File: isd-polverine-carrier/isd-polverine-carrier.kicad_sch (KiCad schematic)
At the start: 21 parts, among them J1 BATT, J3 Conn_01x02_Pin, J4 Conn_01x08_Socket, J5 Conn_01x08_Socket, Q1 Q_Dual_NMOS_S1G1D2S2G2D1, U1 DW01A, U5 AP2112K-3.3, U6 MCP73831-2-OT

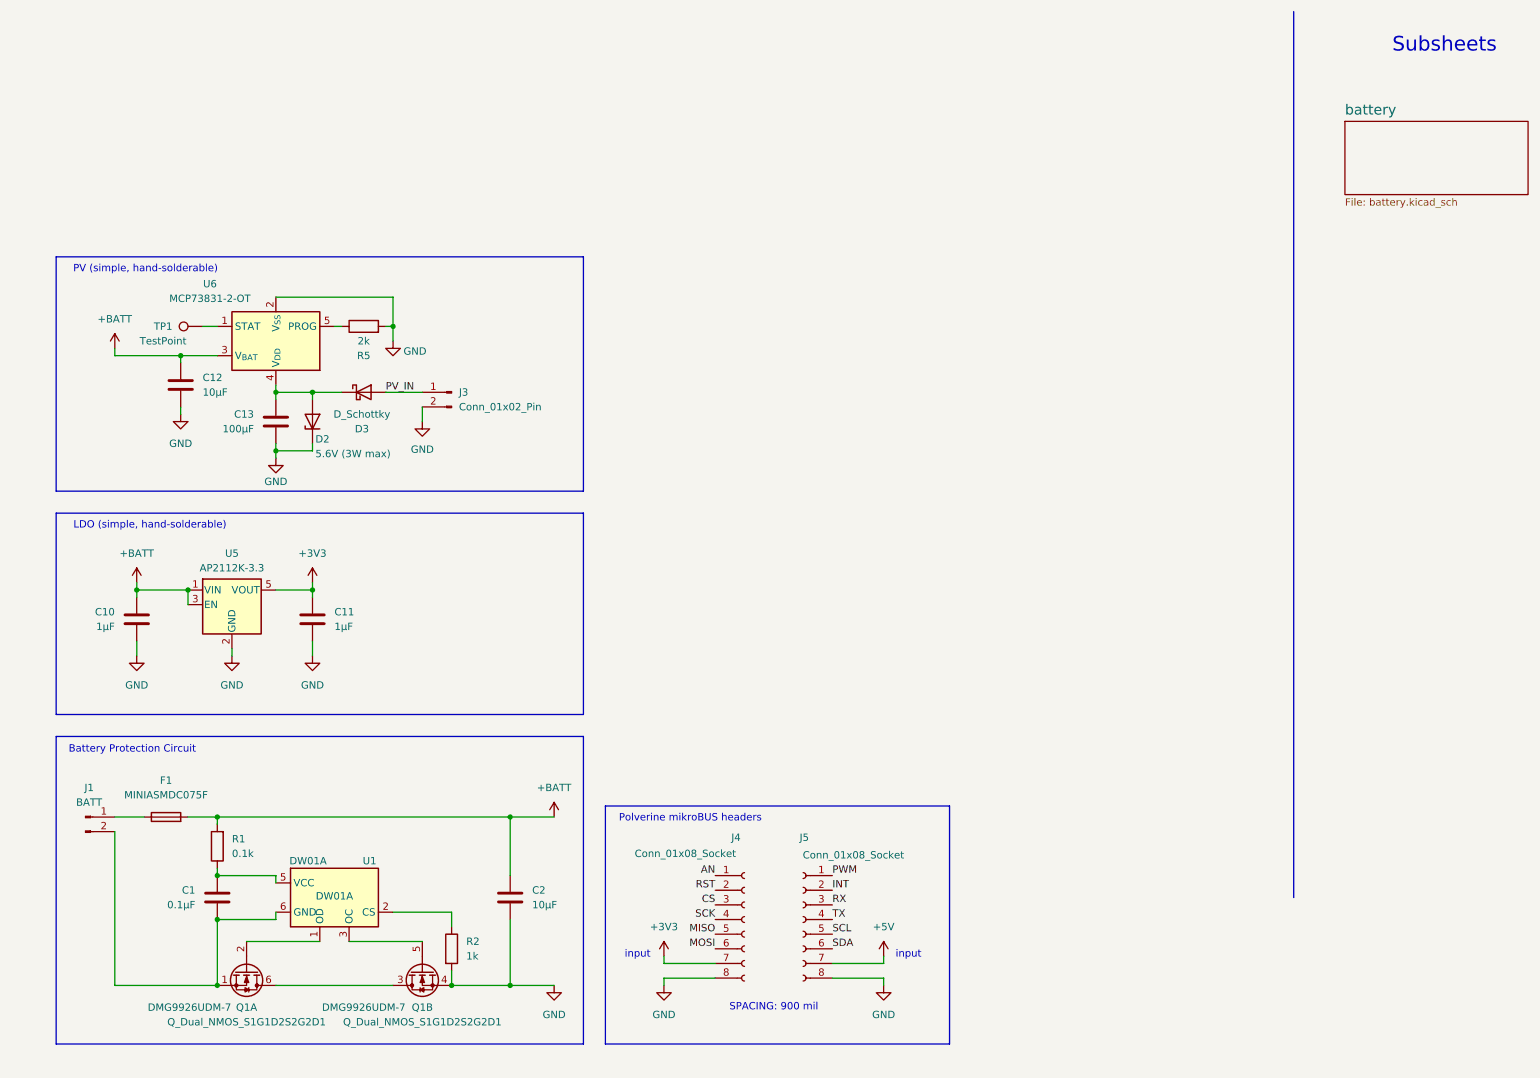
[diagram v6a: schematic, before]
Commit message: add: USB-port for charging, carrier headers, battery monitoring
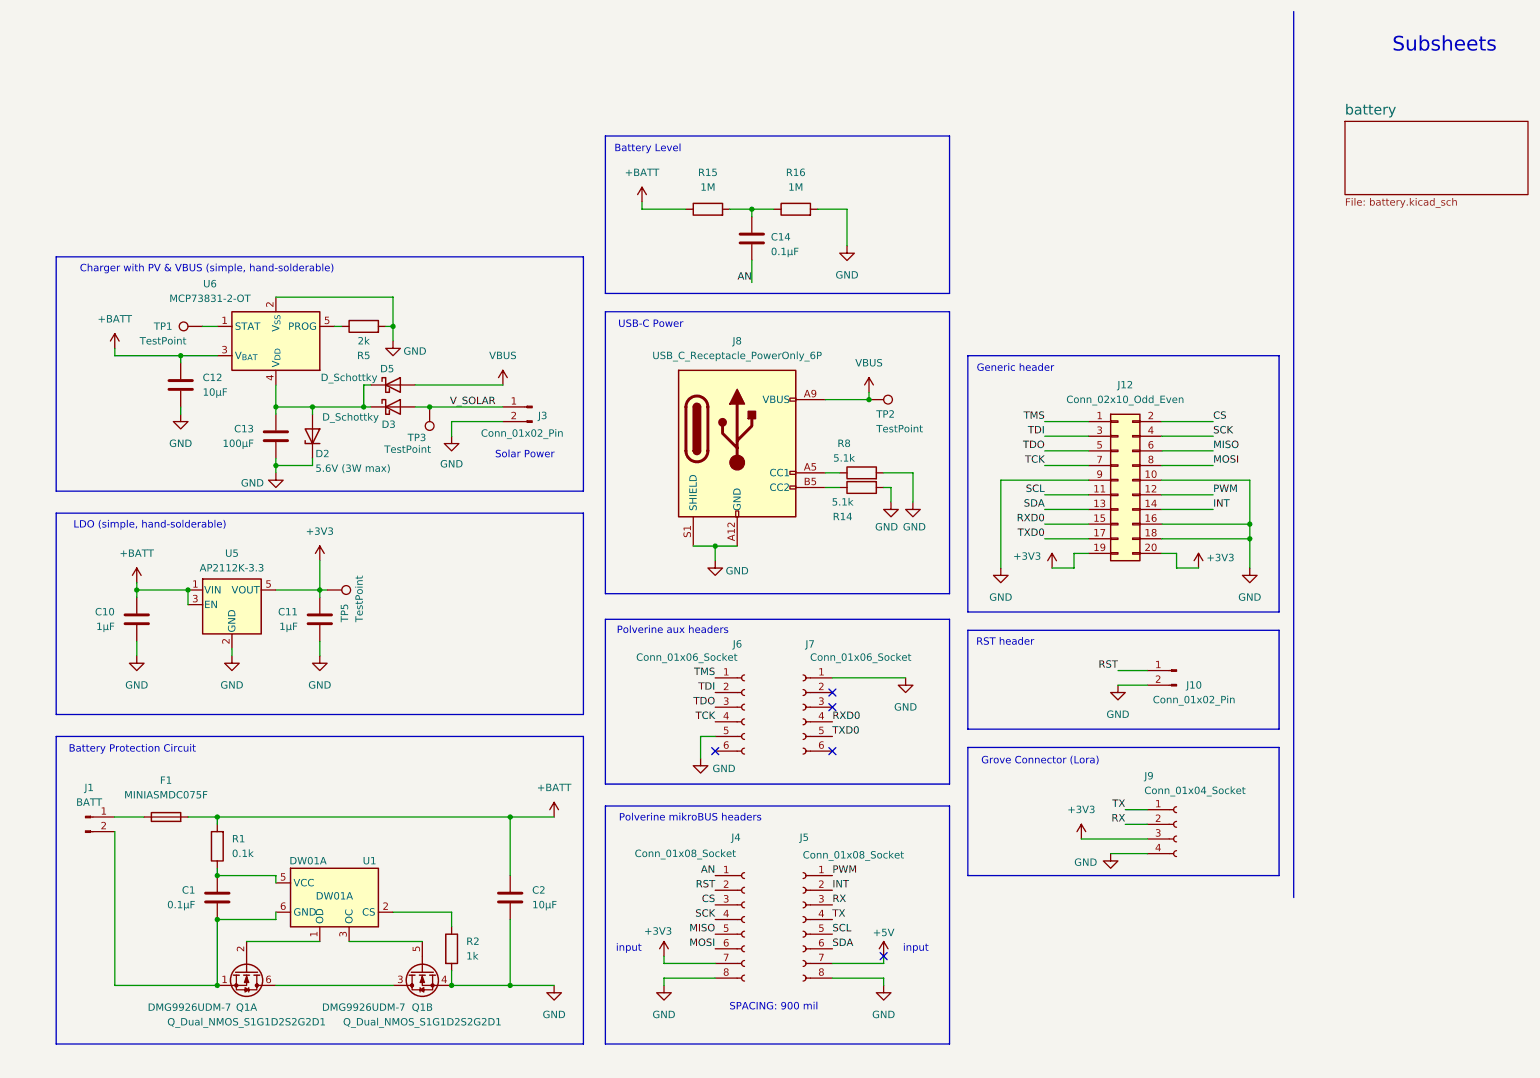
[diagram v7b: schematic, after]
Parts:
- added C14: 0.1µF, symbol Device:C
- added D5: D_Schottky, symbol Device:D_Schottky
- added J10: Conn_01x02_Pin, Connector_PinHeader_2.54mm:PinHeader_1x02_P2.54mm_Vertical, symbol Connector:Conn_01x02_Pin
- added J12: Conn_02x10_Odd_Even, symbol Connector_Generic:Conn_02x10_Odd_Even
- added J6, J7: Conn_01x06_Socket, symbol Connector:Conn_01x06_Socket
- added J8: USB_C_Receptacle_PowerOnly_6P, Connector_USB:USB_C_Receptacle_GCT_USB4125-xx-x-0190_6P_TopMnt_Horizontal, symbol Connector:USB_C_Receptacle_PowerOnly_6P
- added J9: Conn_01x04_Socket, Connector:NS-Tech_Grove_1x04_P2mm_Vertical, symbol Connector:Conn_01x04_Socket
- added R14, R8: 5.1k, symbol Device:R
- added R15, R16: 1M, symbol Device:R
- added TP2, TP3, TP5: TestPoint, symbol Connector:TestPoint
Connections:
- net +3V3: now also J12.19 (Pin_19), J12.20 (Pin_20), J9.3 (Pin_3), TP5.1
- net +BATT: now also R15.1
- net AN: now also C14.2
- net CS: now also J12.2 (Pin_2)
- net GND: now also J10.2 (Pin_2), J12.10 (Pin_10), J12.16 (Pin_16), J12.18 (Pin_18), J12.9 (Pin_9), J6.5 (Pin_5), J7.1 (Pin_1), J8.A12 (GND), J8.B12 (GND), J8.S1 (SHIELD), J9.4 (Pin_4), R14.2, R16.2, R8.2
- net INT: now also J12.14 (Pin_14)
- net MISO: now also J12.6 (Pin_6)
- net MOSI: now also J12.8 (Pin_8)
- net PWM: now also J12.12 (Pin_12)
- net RST: now also J10.1 (Pin_1)
- net RX: now also J9.2 (Pin_2)
- net SCK: now also J12.4 (Pin_4)
- net SCL: now also J12.11 (Pin_11)
- net SDA: now also J12.13 (Pin_13)
- net TX: now also J9.1 (Pin_1)
- net at C13.1, D2.2 (A), D3.1 (K)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: now also D5.1 (K)
- net PV_IN renamed V_SOLAR
- net V_SOLAR: now also TP3.1
- new net: C14.1, R15.2, R16.1
- new net: J8.A5 (CC1), R8.1
- new net: J8.B5 (CC2), R14.1
- new net RXD0: J12.15 (Pin_15), J7.4 (Pin_4)
- new net TCK: J12.7 (Pin_7), J6.4 (Pin_4)
- new net TDI: J12.3 (Pin_3), J6.2 (Pin_2)
- new net TDO: J12.5 (Pin_5), J6.3 (Pin_3)
- new net TMS: J12.1 (Pin_1), J6.1 (Pin_1)
- new net TXD0: J12.17 (Pin_17), J7.5 (Pin_5)
- new net VBUS: D5.2 (A), J8.A9 (VBUS), J8.B9 (VBUS), TP2.1
- no-connect marks 0 -> 5
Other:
- note added: "Battery Level"
- note added: "Charger with PV & VBUS (simple, hand-solderable)"
- note added: "Generic header"
- note added: "Grove Connector (Lora)"
- note added: "Polverine aux headers"
- note added: "RST header"
- note added: "Solar Power"
- note added: "USB-C Power"
- note removed: "PV (simple, hand-solderable)"
- moved on the sheet: C11, C13, D2, D3, J3

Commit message: Added P Mos to solar charger controller for load sharing
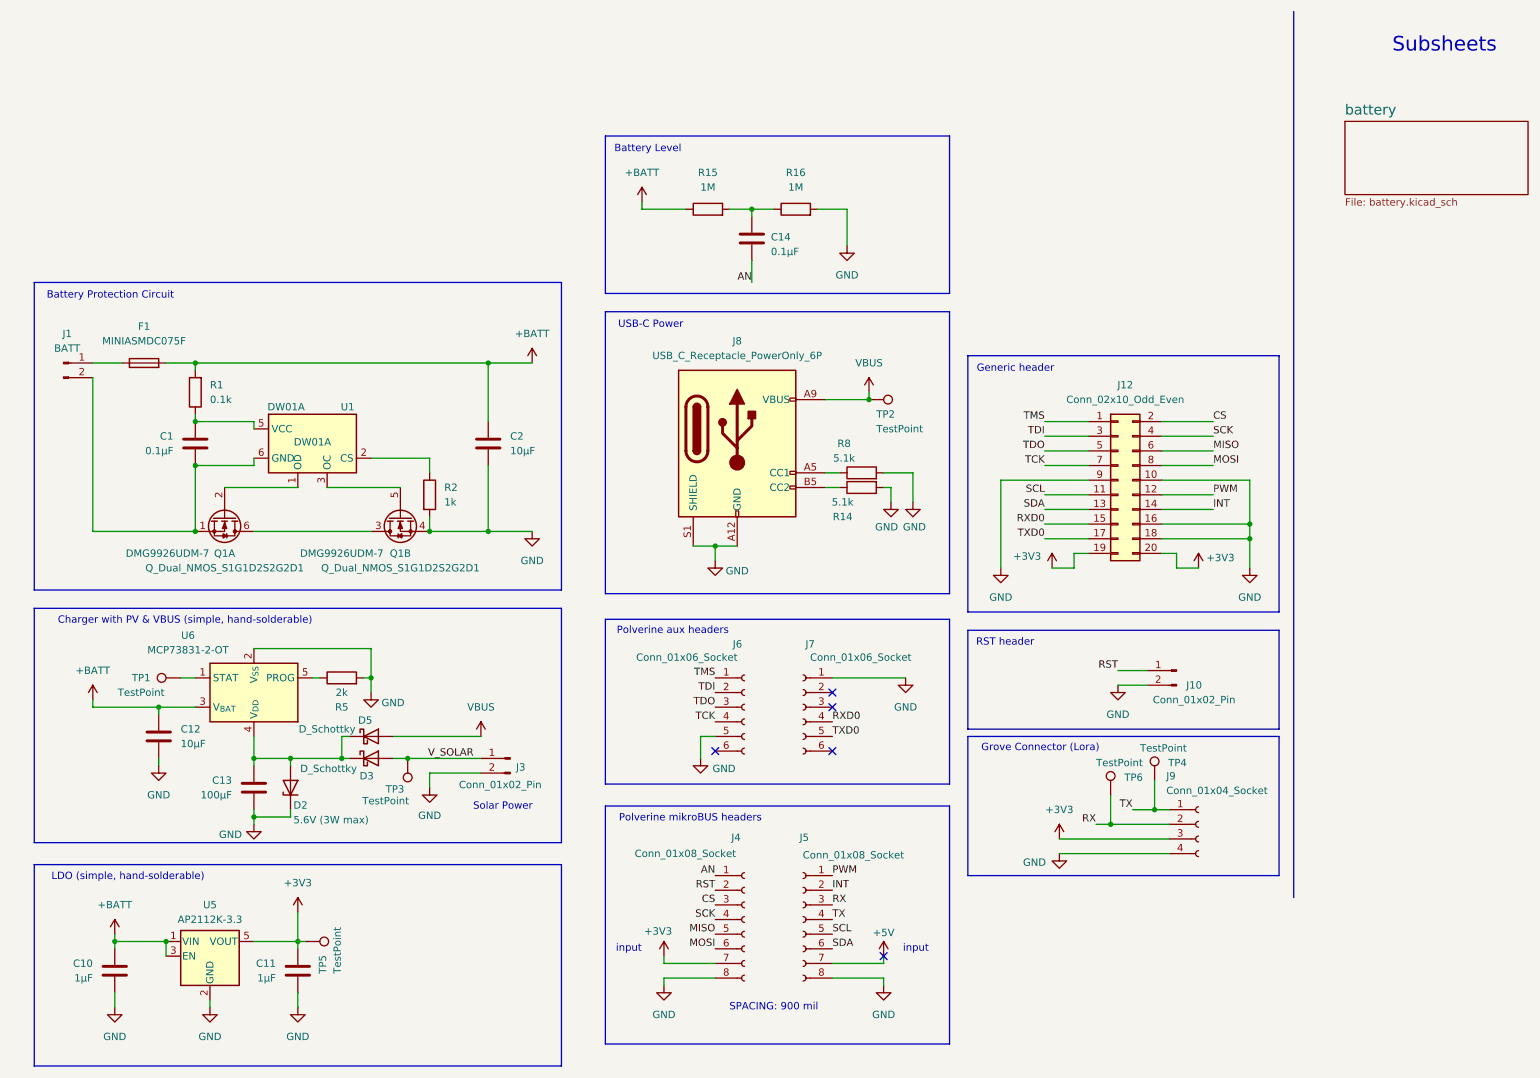
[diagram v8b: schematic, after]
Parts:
- added TP4, TP6: TestPoint, symbol Connector:TestPoint
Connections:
- net RX: now also TP6.1
- net TX: now also TP4.1
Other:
- moved on the sheet: C1, C10, C11, C12, C13, C2, D2, D3, D5, F1, J1, J3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
